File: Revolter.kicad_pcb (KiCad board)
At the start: 4 copper layers, 152 x 139 mm, 161 parts, among them IC1 ADM3052, IC2 TPS65320C, IC4 INA240A1, IC5 INA240A1, P1 USB_B, P2 Interface, P3 IN+, P4 IN-, P5 MOTOR3, P6 MOTOR2, P7 MOTOR1, P8 SWD, Q1 ZXTC2045E6, Q10 ZXTC2045E6, Q11 IRFP4668PBF, Q12 IRFP4668PBF, Q2 ZXTC2045E6, Q3 IRFP4668PBF, Q4 IRFP4668PBF, Q5 ZXTC2045E6, Q6 ZXTC2045E6, Q7 IRFP4668PBF, Q8 IRFP4668PBF, Q9 ZXTC2045E6, U1 STM32F40X_LQFP64, U2 IR2110S, U3 IR2110S, U4 IR2110S, X1 8MHz 10ppm

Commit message: - removed 1 MOSFET of each group (no space) - removed 2 DC buffer caps (no space) - power stage routed - shunts and amps routed - post driver routed - pre driver HV routed
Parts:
- removed B1: MTC1, alexmod:MTC1
- removed C1: 100n, Capacitors_SMD:C_0805
- removed C47: 10u, Capacitors_SMD:C_0805
- removed C50, C53: 330u 250V, alexmod:C_Radial_D22_P10
- removed D1: SS14, Diodes_SMD:SMA_Standard
- removed D9: D_Schottky, Diodes_SMD:SMA_Standard
- removed IC5: INA240A1, Housings_SSOP:TSSOP-8_4.4x3mm_Pitch0.65mm
- removed Q11, Q12: IRFP4668PBF, alexmod:TO-264_flat_reverse
- removed the REF** at (213.0, 157.0)
- removed the REF** at (213.0, 32.0)
- removed the REF** at (73.0, 32.0)
- removed the REF** at (73.0, 157.0)
- added D10: 3V3, Diodes_SMD:D_SOD-123, F.Cu at (232.1, 151.5)
- added D11: 3V3, Diodes_SMD:D_SOD-123, F.Cu at (192.2, 151.5)
- added D12: 3V3, Diodes_SMD:D_SOD-123, F.Cu at (225.4, 151.5)
- added D13: 3V3, Diodes_SMD:D_SOD-123, F.Cu at (198.8, 151.5)
- added IC3: INA181A1, TO_SOT_Packages_SMD:SOT-23-6, B.Cu at (63.0, 92.0)
- added L2: NRH2410T100MN, alexmod:NRH2410, F.Cu at (332.0, 62.0)
- added P10: AUX, Connectors_Terminal_Blocks:TerminalBlock_Pheonix_PT-3.5mm_7pol, F.Cu at (340.0, 87.0)
- added P9: Motor, Connectors_Terminal_Blocks:TerminalBlock_Pheonix_PT-3.5mm_6pol, F.Cu at (576.5, 41.0)
- added Q13: IRFB4110, alexmod:TO220GDS_notab_rev, B.Cu at (90.0, 74.5)
- added Q14: IRFB4110, alexmod:TO220GDS_notab_rev, B.Cu at (80.0, 88.0)
- added Q15: IRFB4110, alexmod:TO220GDS_notab_rev, B.Cu at (90.0, 85.5)
- added Q16: IRFB4110, alexmod:TO220GDS_notab_rev, B.Cu at (80.0, 77.0)
- added Q19: IRFB4110, alexmod:TO220GDS_notab_rev, B.Cu at (90.0, 96.5)
- added Q20: IRFB4110, alexmod:TO220GDS_notab_rev, B.Cu at (80.0, 110.0)
- added Q21: IRFB4110, alexmod:TO220GDS_notab_rev, B.Cu at (90.0, 107.5)
- added Q22: IRFB4110, alexmod:TO220GDS_notab_rev, B.Cu at (80.0, 99.0)
- added R45: 10k, Resistors_SMD:R_0805, B.Cu at (66.2, 67.2)
- added R46: 10k, Resistors_SMD:R_0805, B.Cu at (66.2, 63.8)
- added R59: 1R, Resistors_SMD:R_0805, F.Cu at (93.0, 105.0)
- added R60: 1R, Resistors_SMD:R_0805, F.Cu at (77.0, 101.5)
- added REF**: MountingHole_3.2mm_M3_DIN965, Mounting_Holes:MountingHole_3.2mm_M3_DIN965, F.Cu at (63.0, 137.0)
- added REF**: MountingHole_3.2mm_M3_DIN965, Mounting_Holes:MountingHole_3.2mm_M3_DIN965, F.Cu at (99.0, 120.0)
- added REF**: MountingHole_3.2mm_M3_DIN965, Mounting_Holes:MountingHole_3.2mm_M3_DIN965, F.Cu at (71.0, 120.0)
- added REF**: MountingHole_3.2mm_M3_DIN965, Mounting_Holes:MountingHole_3.2mm_M3_DIN965, F.Cu at (99.0, 45.0)
- added REF**: MountingHole_3.2mm_M3_DIN965, Mounting_Holes:MountingHole_3.2mm_M3_DIN965, F.Cu at (71.0, 45.0)
- added REF**: MountingHole_3.2mm_M3_DIN965, Mounting_Holes:MountingHole_3.2mm_M3_DIN965, F.Cu at (63.0, 45.0)
- added U5: PCA82C251, Housings_SOIC:SOIC-8_3.9x4.9mm_Pitch1.27mm, F.Cu at (349.7, 40.1)
- added U6: 7805_SO8, Housings_SOIC:SOIC-8_3.9x4.9mm_Pitch1.27mm, F.Cu at (155.3, 152.1)
- C10, C48: value 10u -> 22u
- C18, C19, C20, C23, C24, C25, C26: moved to F.Cu
- C27, C28: value 22u -> 100n; footprint Capacitors_SMD:C_1206 -> Capacitors_SMD:C_0805
- C29: value 100u 16V -> 47u 120V; footprint Capacitors_ThroughHole:C_Radial_D6.3_L11.2_P2.5 -> Capacitors_THT:CP_Radial_D6.3mm_P2.50mm
- C31: value 3n3 -> 100n
- C39, C41, C43, C44: moved to B.Cu
- C40, C42: value opt -> 100n; moved to B.Cu
- C45: value 10p -> 22u
- C46: value 5n6 -> 3n3
- C49: value 100u 6V3 -> 100u 22V; footprint Capacitors_ThroughHole:C_Radial_D6.3_L11.2_P2.5 -> Capacitors_THT:CP_Radial_D6.3mm_P2.50mm
- C51: value 330u 250V -> 1mF 100V
- C9: value 1u -> 100n
- D5, D6, D7: value RFN2L4S -> BAS21L; footprint Diodes_SMD:SMA_Standard -> Diodes_SMD:D_SOT-23_ANK
- D8: value D_Schottky -> 4148; footprint Diodes_SMD:SMA_Standard -> Diodes_SMD:D_MiniMELF_Standard
- IC1: value ADM3052 -> LM5017; footprint Housings_SOIC:SOIC-16_7.5x10.3mm_Pitch1.27mm -> Housings_SOIC:SOIC-8-1EP_3.9x4.9mm_Pitch1.27mm
- IC2: value TPS65320C -> AP65111; footprint alexmod:TSSOP-14_4.4x5mm_Pitch0.65mm_EP -> TO_SOT_Packages_SMD:SOT-23-6
- IC4: value INA240A1 -> INA181A1; footprint Housings_SSOP:TSSOP-8_4.4x3mm_Pitch0.65mm -> TO_SOT_Packages_SMD:SOT-23-6; moved to B.Cu
- L1: value SRR6038-3R3Y -> VLS6045EX-221M; footprint alexmod:SRR6038 -> alexmod:VLS6045EX
- P1: footprint alexmod:USBB_vert -> Connectors_USB:USB_Micro-B_Molex-105017-0001
- P2: value Interface -> CAN; footprint alexmod:XG4A_20_wo_56 -> Connectors_Terminal_Blocks:TerminalBlock_Pheonix_PT-3.5mm_4pol
- P3, P4, P5, P6, P7: footprint Mounting_Holes:MountingHole_6.5mm_Pad_Via -> Mounting_Holes:MountingHole_3.2mm_M3_Pad_Via
- P8: footprint Pin_Headers:Pin_Header_Straight_2x03 -> Pin_Headers:Pin_Header_Straight_2x03_Pitch2.54mm
- Q3, Q4, Q7, Q8: value IRFP4668PBF -> IRFB4110; footprint alexmod:TO-264_flat_reverse -> alexmod:TO220GDS_notab_rev
- R3: value 2k2 -> 1R
- R30: value 120R -> 76k
- R31: value 300R -> 10k; footprint Resistors_SMD:R_1206 -> Resistors_SMD:R_0805
- R39: value 52k3 -> 499k
- R40: value 28k -> 59k
- R41: value 30k1 -> 46k4
- R42: value 95k3 -> 40k2
- R43: value 18k2 -> 1k
- R44: value 95k3 -> 10k
- R47, R48: value CSS2H-3920R-L500 -> WSLF2512L5000FEB; moved to F.Cu
- R49: value opt -> 13k
- R50, R51, R52: value opt -> 1R
- R54, R56, R58: value k -> 12k
- R7: value 160k -> 100k
- U2, U3, U4: footprint Housings_SOIC:SOIC-16_7.5x10.3mm_Pitch1.27mm -> Housings_SOIC:SOIC-16W_7.5x10.3mm_Pitch1.27mm
- moved P2 512.4 mm to (576.5, 29.0), turned to 0 degrees
- moved X1 421.4 mm to (558.1, 34.0), turned to 0 degrees
- moved C12 378.8 mm to (479.1, 175.5), turned to 0 degrees
- moved C14 377.2 mm to (458.6, 175.5), turned to 0 degrees
- moved C13 357.6 mm to (472.3, 175.5), turned to 0 degrees
- moved C10 355.9 mm to (438.0, 175.5), turned to 0 degrees
- moved R54 345.0 mm to (445.0, 152.0), turned to 0 degrees
- moved C11 343.1 mm to (425.3, 119.5), turned to 0 degrees
- moved R31 334.9 mm to (418.4, 151.5)
- moved C24 315.4 mm to (451.7, 175.5), turned to 0 degrees
- moved C28 315.2 mm to (417.7, 119.5), turned to 0 degrees
- moved C17 289.3 mm to (444.9, 175.5), turned to 0 degrees
- moved R4 286.8 mm to (431.7, 151.5), turned to 0 degrees
- moved R30 285.2 mm to (371.8, 151.5), turned to 0 degrees
- moved R5 282.1 mm to (425.0, 151.5), turned to 0 degrees
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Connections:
- C10 pad 1: Earth -> +12V
- C10 pad 2: Net-(C10-Pad2) -> GND
- C11 pad 1: +12VA -> +12V
- C11 pad 2: Earth -> GND
- C12 pad 1: +3V3 -> Net-(C12-Pad1)
- C12 pad 2: GND -> Net-(C12-Pad2)
- C27 pad 1: +12VA -> +5V
- C27 pad 2: Earth -> GND
- C28 pad 1: +12V -> Net-(C28-Pad1)
- C28 pad 2: GND -> Net-(C28-Pad2)
- C29 pad 1: +12V -> Net-(C29-Pad1)
- C30 pad 1: +12V -> Net-(C29-Pad1)
- C40 pad 1: Net-(C40-Pad1) -> U/2
- C40 pad 2: Net-(C40-Pad2) -> GND
- C42 pad 1: Net-(C42-Pad1) -> U/2
- C42 pad 2: Net-(C42-Pad2) -> GND
- C45 pad 1: GND -> +3V3
- C45 pad 2: Net-(C45-Pad2) -> GND
- C46 pad 1: GND -> +12V
- C46 pad 2: Net-(C46-Pad2) -> Net-(C28-Pad2)
- C48 pad 1: +5V -> +12V
- C49 pad 1: +5V -> +12V
- C9 pad 1: Net-(C9-Pad1) -> +5V
- C9 pad 2: Earth -> GND
- D8 pad 1: Net-(D8-Pad1) -> Net-(C31-Pad1)
- D8 pad 2: NRST -> +12V
- IC1 pad 1: (no net) -> GND
- IC1 pad 2: GND -> Net-(C29-Pad1)
- IC1 pad 3: GND -> Net-(IC1-Pad3)
- IC1 pad 4: (no net) -> Net-(IC1-Pad4)
- IC1 pad 5: /CAN bus transceiver/CAN_RX -> Net-(C28-Pad1)
- IC1 pad 6: /CAN bus transceiver/CAN_TX -> Net-(C31-Pad1)
- IC1 pad 7: +3V3 -> Net-(C32-Pad1)
- IC1 pad 8: GND -> Net-(C32-Pad2)
- IC1 pad 9: Earth -> GND
- IC2 pad 1: Net-(C32-Pad1) -> +12V
- IC2 pad 2: +12V -> Net-(C12-Pad2)
- IC2 pad 3: +5V -> GND
- IC2 pad 4: +3V3 -> Net-(C12-Pad1)
- IC2 pad 5: Net-(IC2-Pad5) -> +12V
- IC2 pad 6: Net-(D8-Pad1) -> Net-(IC2-Pad6)
- IC4 pad 1: (no net) -> /MCU/BR_SO2
- IC4 pad 2: Net-(C40-Pad1) -> GND
- IC4 pad 3: Net-(C40-Pad2) -> /Mosfet driver/H1_LOW
- IC4 pad 4: GND -> GNDPWR
- IC4 pad 5: +3V3 -> U/2
- L1 pad 1: +5V -> +12V
- P1 pad 1: Net-(D1-Pad2) -> (no net)
- P2 pad 1: +12VA -> GND
- P2 pad 2: /CAN bus transceiver/CANH -> /CAN bus transceiver/CANL
- P2 pad 3: /CAN bus transceiver/CANL -> /CAN bus transceiver/CANH
- P2 pad 4: Earth -> (no net)
- Q7 pad 3: /Mosfet driver/H2_VS -> /Mosfet driver/H1_VS
- Q8 pad 2: /Mosfet driver/H2_VS -> /Mosfet driver/H1_VS
- Q8 pad 3: GNDPWR -> /Mosfet driver/H1_LOW
- R22 pad 1: Net-(Q7-Pad1) -> Net-(Q13-Pad1)
- R23 pad 1: Net-(Q8-Pad1) -> Net-(Q14-Pad1)
- R3 pad 1: Net-(P2-Pad19) -> Net-(Q7-Pad1)
- R3 pad 2: /MCU/SERVO -> Net-(Q1-Pad4)
- R30 pad 1: /CAN bus transceiver/CANH -> Net-(IC1-Pad3)
- R30 pad 2: /CAN bus transceiver/CANL -> Net-(C29-Pad1)
- R31 pad 1: Net-(C10-Pad2) -> GND
- R31 pad 2: +12VA -> Net-(IC1-Pad3)
- R32 pad 2: +3V3 -> +5V
- R33 pad 2: +3V3 -> +5V
- R34 pad 2: +3V3 -> +5V
- R35 pad 2: +3V3 -> +5V
- R39 pad 1: Net-(IC2-Pad9) -> Net-(IC1-Pad4)
- R39 pad 2: GND -> Net-(C29-Pad1)
- R40 pad 1: Net-(C46-Pad2) -> Net-(R40-Pad1)
- R40 pad 2: Net-(C45-Pad2) -> Net-(IC2-Pad6)
- R41 pad 1: Net-(IC2-Pad5) -> Net-(C28-Pad2)
- R41 pad 2: GND -> Net-(C32-Pad2)
- R42 pad 2: Net-(IC2-Pad5) -> Net-(R40-Pad1)
- R43 pad 1: Net-(IC2-Pad11) -> Net-(C28-Pad1)
- R44 pad 1: +5V -> Net-(C28-Pad1)
- R44 pad 2: Net-(IC2-Pad11) -> +12V
- R49 pad 1: Net-(C40-Pad1) -> Net-(R40-Pad1)
- R49 pad 2: /Mosfet driver/H3_LOW -> GND
- R50 pad 1: Net-(C40-Pad2) -> Net-(Q8-Pad1)
- R50 pad 2: GNDPWR -> Net-(Q2-Pad4)
- R51 pad 1: Net-(C42-Pad1) -> Net-(Q15-Pad1)
- R51 pad 2: /Mosfet driver/H1_LOW -> Net-(Q5-Pad4)
- R52 pad 1: Net-(C42-Pad2) -> Net-(Q16-Pad1)
- R52 pad 2: GNDPWR -> Net-(Q6-Pad4)
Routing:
- net (no net): track 571.9 -> 100.0 mm, vias 0 -> 15
- net +12V: track 373.4 -> 186.3 mm, vias 2 -> 4
- net /MCU/EN_GATE: track 141.6 -> 0.00 mm, vias 2 -> 0
- net /Filters/TEMP_IN: track 116.3 -> 0.00 mm, vias 2 -> 0
- net +3V3: track 125.8 -> 10.6 mm, vias 17 -> 0
- net GND: track 142.4 -> 31.9 mm, vias 50 -> 0
- net GNDPWR: track 77.1 -> 187.1 mm, vias 4 -> 45
- net /MCU/RX_SCL_MOSI: track 103.1 -> 0.00 mm, vias 3 -> 0
- net /MCU/TX_SDA_NSS: track 99.3 -> 0.00 mm, vias 2 -> 0
- net /MCU/ADC_TEMP: track 95.7 -> 0.00 mm, vias 4 -> 0
- net +BATT: track 44.1 -> 139.2 mm
- net /Filters/HALL2_OUT: track 94.7 -> 0.00 mm
- net /Filters/HALL1_OUT: track 88.6 -> 0.00 mm
- net /MCU/BR_SO1: track 88.5 -> 0.00 mm, vias 4 -> 0
- net /MCU/SCK_ADC_EXT: track 87.3 -> 0.00 mm, vias 2 -> 0
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- removed copper zone on Power1, net +3V3
- removed copper zone on B.Cu, net +BATT
- removed copper zone on B.Cu, net /Mosfet driver/H1_LOW
- removed copper zone on Power1, net /Mosfet driver/H1_VS
- removed copper zone on Power1, net /Mosfet driver/H2_VS
- removed copper zone on B.Cu, net /Mosfet driver/H3_LOW
- removed copper zone on Power1, net /Mosfet driver/H3_VS
- removed copper zone on GND, net GND
- removed copper zone on B.Cu, net GNDPWR
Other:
- board size 152 x 139 mm -> 100 x 100 mm
- copper layers 4 -> 2
- rule pad_to_mask_clearance: 0.2 -> 0
- board text removed: "+"
- board text removed: "-"
- board text removed: "1"
- board text removed: "2"
- board text removed: "3"
- board text removed: "4"
- board text removed: "HSWR V2.0 200V 100A *20170301 Alexander Schröder"
- board text removed: "U"
- board text removed: "V"
- board text removed: "W"

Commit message: - redesigned the MOSFET mounting -> minor changes to the power stage - logic and interface routed -> layout finished - needs final check and gerber export
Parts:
- removed C29: 47u 120V, Capacitors_THT:CP_Radial_D6.3mm_P2.50mm
- removed R11: R, Resistors_SMD:R_0805
- removed the REF** at (99.0, 120.0)
- removed the REF** at (71.0, 120.0)
- removed the REF** at (99.0, 45.0)
- removed the REF** at (71.0, 45.0)
- added JP1: JUMPER, alexmod:Jumper_2, F.Cu at (98.8, 125.2)
- added REF**: MountingHole_3.2mm_M3_DIN965, Mounting_Holes:MountingHole_3.2mm_M3_DIN965, F.Cu at (155.0, 45.0)
- added REF**: MountingHole_3.2mm_M3_DIN965, Mounting_Holes:MountingHole_3.2mm_M3_DIN965, F.Cu at (155.0, 137.0)
- C30: value 10u -> 1u; footprint Capacitors_SMD:C_0805 -> Capacitors_SMD:C_1206
- C39, C40, C41, C42, C43, C44, IC3, IC4, R45, R46: moved to F.Cu
- moved P2 441.4 mm to (148.0, 135.0), turned to 180 degrees
- moved X1 430.6 mm to (127.8, 49.1), turned to 270 degrees
- moved P9 428.2 mm to (153.0, 104.0), turned to 270 degrees
- moved C12 357.4 mm to (125.8, 122.0), turned to 180 degrees
- moved C17 345.1 mm to (123.5, 49.8), turned to 270 degrees
- moved C24 343.5 mm to (127.8, 61.2)
- moved C13 333.9 mm to (145.0, 109.2)
- moved C22 331.1 mm to (123.5, 53.2), turned to 90 degrees
- moved C14 322.7 mm to (140.8, 119.8), turned to 180 degrees
- moved R54 318.3 mm to (132.8, 90.0)
- moved C10 317.9 mm to (125.8, 116.0)
- moved R31 312.0 mm to (106.8, 137.2), turned to 90 degrees
- moved R4 308.8 mm to (134.2, 68.5), turned to 90 degrees
- moved C2 308.2 mm to (106.0, 69.2), turned to 90 degrees
- moved R5 298.6 mm to (138.2, 68.5), turned to 90 degrees
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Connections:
- C30 pad 1: Net-(C29-Pad1) -> +BATT
- IC1 pad 2: Net-(C29-Pad1) -> +BATT
- P2 pad 4: (no net) -> +12V
- R30 pad 2: Net-(C29-Pad1) -> +BATT
- R39 pad 2: Net-(C29-Pad1) -> +BATT
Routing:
- net +3V3: track 10.6 -> 404.2 mm, vias 0 -> 13
- net GND: track 31.9 -> 311.3 mm, vias 0 -> 29
- net +12V: track 186.3 -> 353.1 mm, vias 4 -> 6
- net /MCU/BR_SO1: track 0.00 -> 146.9 mm, vias 0 -> 2
- net /MCU/BR_SO2: track 0.00 -> 116.1 mm, vias 0 -> 2
- net /Filters/HALL3_OUT: track 0.00 -> 97.0 mm, vias 0 -> 2
- net /MCU/EN_GATE: track 0.00 -> 94.0 mm
- net /CAN bus transceiver/CAN_RX: track 0.00 -> 86.5 mm, vias 0 -> 2
- net /CAN bus transceiver/CAN_TX: track 0.00 -> 83.3 mm, vias 0 -> 2
- net /MCU/H3: track 0.00 -> 78.3 mm, vias 0 -> 2
- net /Filters/TEMP_IN: track 0.00 -> 71.2 mm, vias 0 -> 2
- net /MCU/L3: track 0.00 -> 69.9 mm, vias 0 -> 2
- net NRST: track 0.00 -> 68.1 mm, vias 0 -> 3
- net /Filters/HALL2_OUT: track 0.00 -> 68.0 mm, vias 0 -> 2
- net /Filters/HALL1_OUT: track 0.00 -> 66.3 mm, vias 0 -> 2
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- added copper zone on B.Cu, net GND
- added copper zone on F.Cu, net GND

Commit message: - final check - minor layout cleanups - labeling - first production run => V1.0
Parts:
- P1: value USB_B -> USB_OTG
- moved C35 3.36 mm to (124.2, 84.0), turned to 180 degrees
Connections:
- P1 pad 4: GND -> (no net)
- P1 pad 6: (no net) -> GND
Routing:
- net GND: track 311.3 -> 358.6 mm, vias 29 -> 34
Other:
- rule pad_to_mask_clearance: 0 -> 0.05
- board text added: "*AS20170922 REVOLTER 100V V1.0"

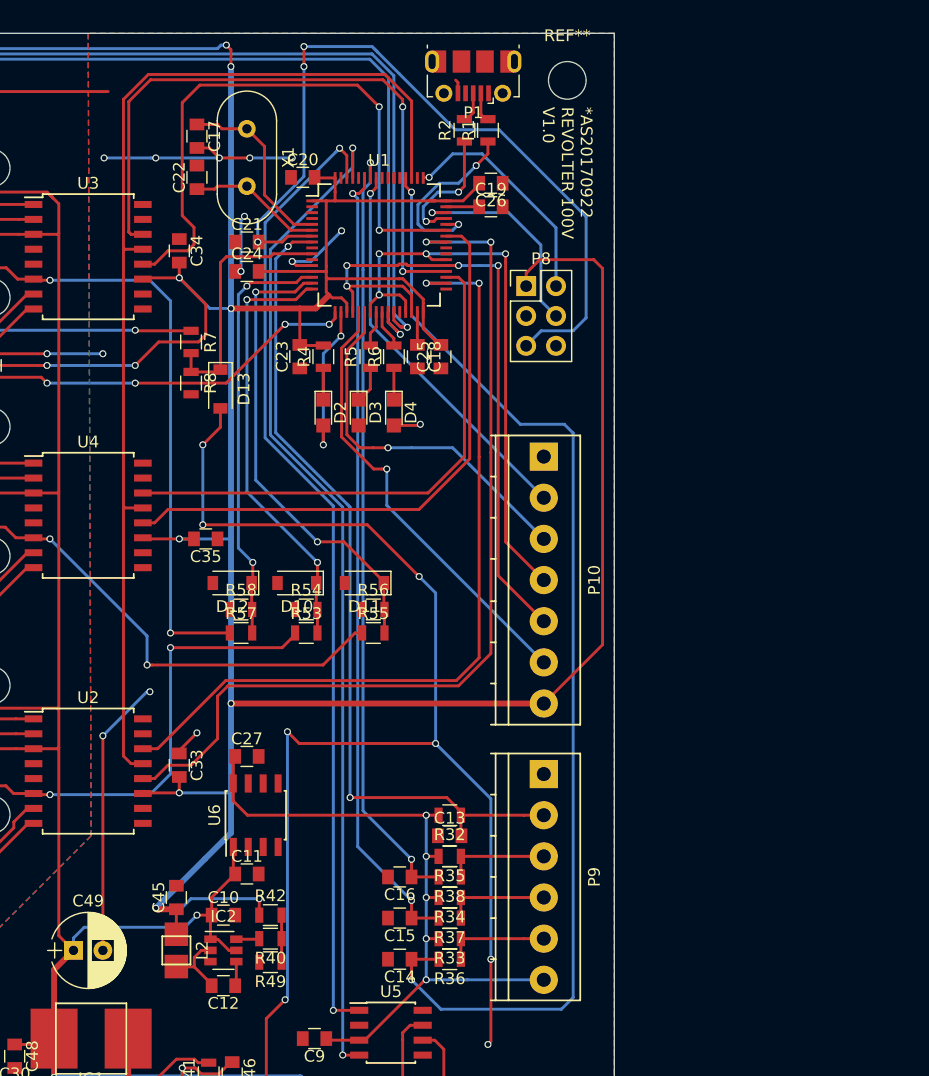
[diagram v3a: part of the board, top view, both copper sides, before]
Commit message: - fixed swapped pins 2 and 3 on IC2 - added optional dividers to ADC inputs - made Vcc selectable between 3V3 or 5V
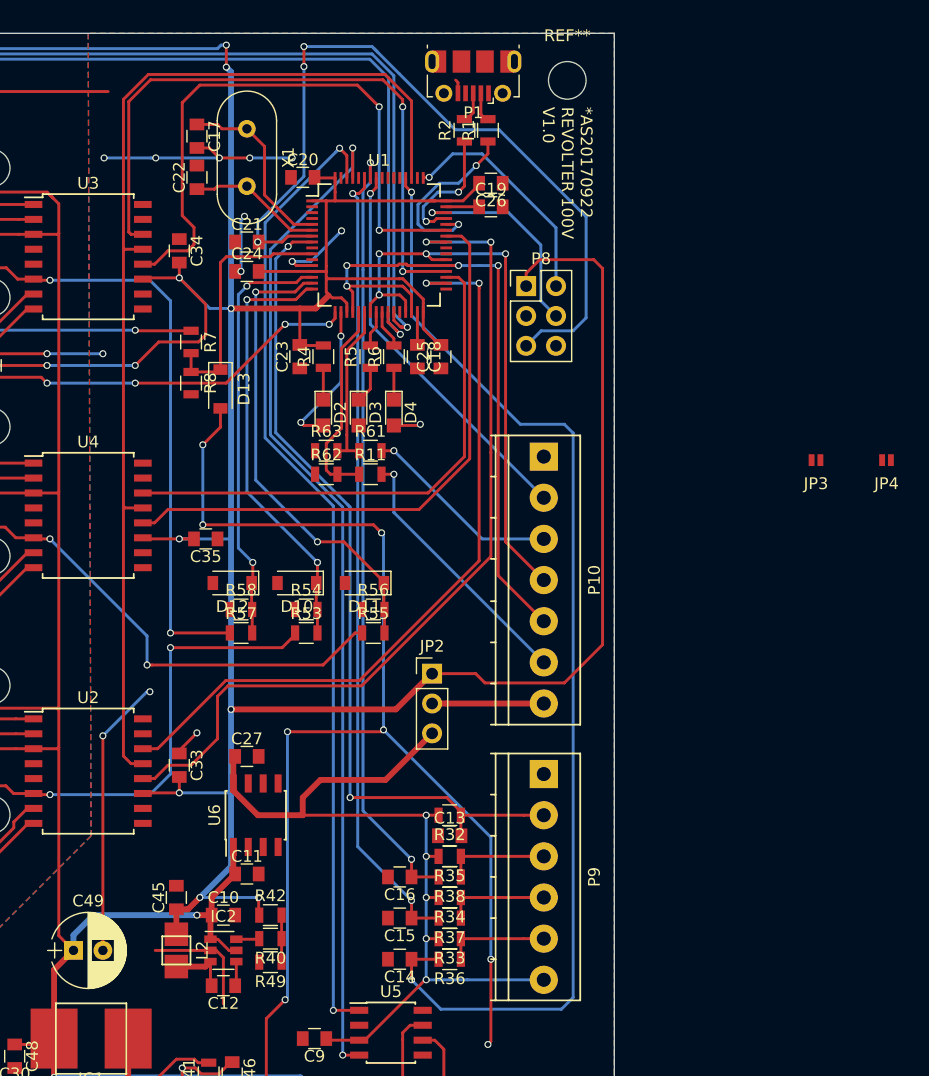
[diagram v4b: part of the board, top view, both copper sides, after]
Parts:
- added JP2: Vcc select, Pin_Headers:Pin_Header_Straight_1x03_Pitch2.54mm, F.Cu at (143.5, 95.5)
- added JP3: opt., alexmod:Jumper_2, F.Cu at (176.2, 77.3)
- added JP4: opt., alexmod:Jumper_2, F.Cu at (182.2, 77.3)
- added R11: 1k, Resistors_SMD:R_0805, F.Cu at (138.2, 78.5)
- added R61: 1k, Resistors_SMD:R_0805, F.Cu at (138.2, 76.5)
- added R62: 1k5, Resistors_SMD:R_0805, F.Cu at (134.5, 78.5)
- added R63: 1k5, Resistors_SMD:R_0805, F.Cu at (134.5, 76.5)
- R30: value 76k -> 82k
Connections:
- IC2 pad 2: Net-(C12-Pad2) -> GND
- IC2 pad 3: GND -> Net-(C12-Pad2)
- P10 pad 3: /MCU/MISO_ADC_EXT2 -> Net-(JP4-Pad1)
- P10 pad 6: /MCU/SCK_ADC_EXT -> Net-(JP3-Pad1)
- P10 pad 7: +3V3 -> Net-(JP2-Pad2)
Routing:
- net Net-(JP3-Pad1): track 0.00 -> 22.3 mm, vias 0 -> 1
- net /MCU/SCK_ADC_EXT: track 38.2 -> 17.5 mm, vias 1 -> 0
- net /MCU/MISO_ADC_EXT2: track 31.5 -> 14.3 mm, vias 1 -> 0
- net Net-(JP4-Pad1): track 0.00 -> 16.9 mm, vias 0 -> 1
- net +5V: track 59.6 -> 73.9 mm
- net Net-(JP2-Pad2): track 0.00 -> 9.50 mm
- net +3V3: track 404.0 -> 399.0 mm
- net /MCU/H3: track 78.3 -> 73.5 mm
- net /MCU/L3: track 69.9 -> 65.0 mm
- net GND: track 358.6 -> 363.4 mm
- net Net-(C12-Pad2): track 6.17 -> 5.17 mm
